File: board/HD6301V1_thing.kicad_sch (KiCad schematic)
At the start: 51 parts, among them J1 KMDGX-6S-BS, J2 ps2_i2c, J3 P1_connector, J4 memmap_i2c, J5 8bit_thing_bus_connector, J6 USB_B_Micro, J7 prog_LED, J8 pwr_LED, SW1 Reset, SW2 Banking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

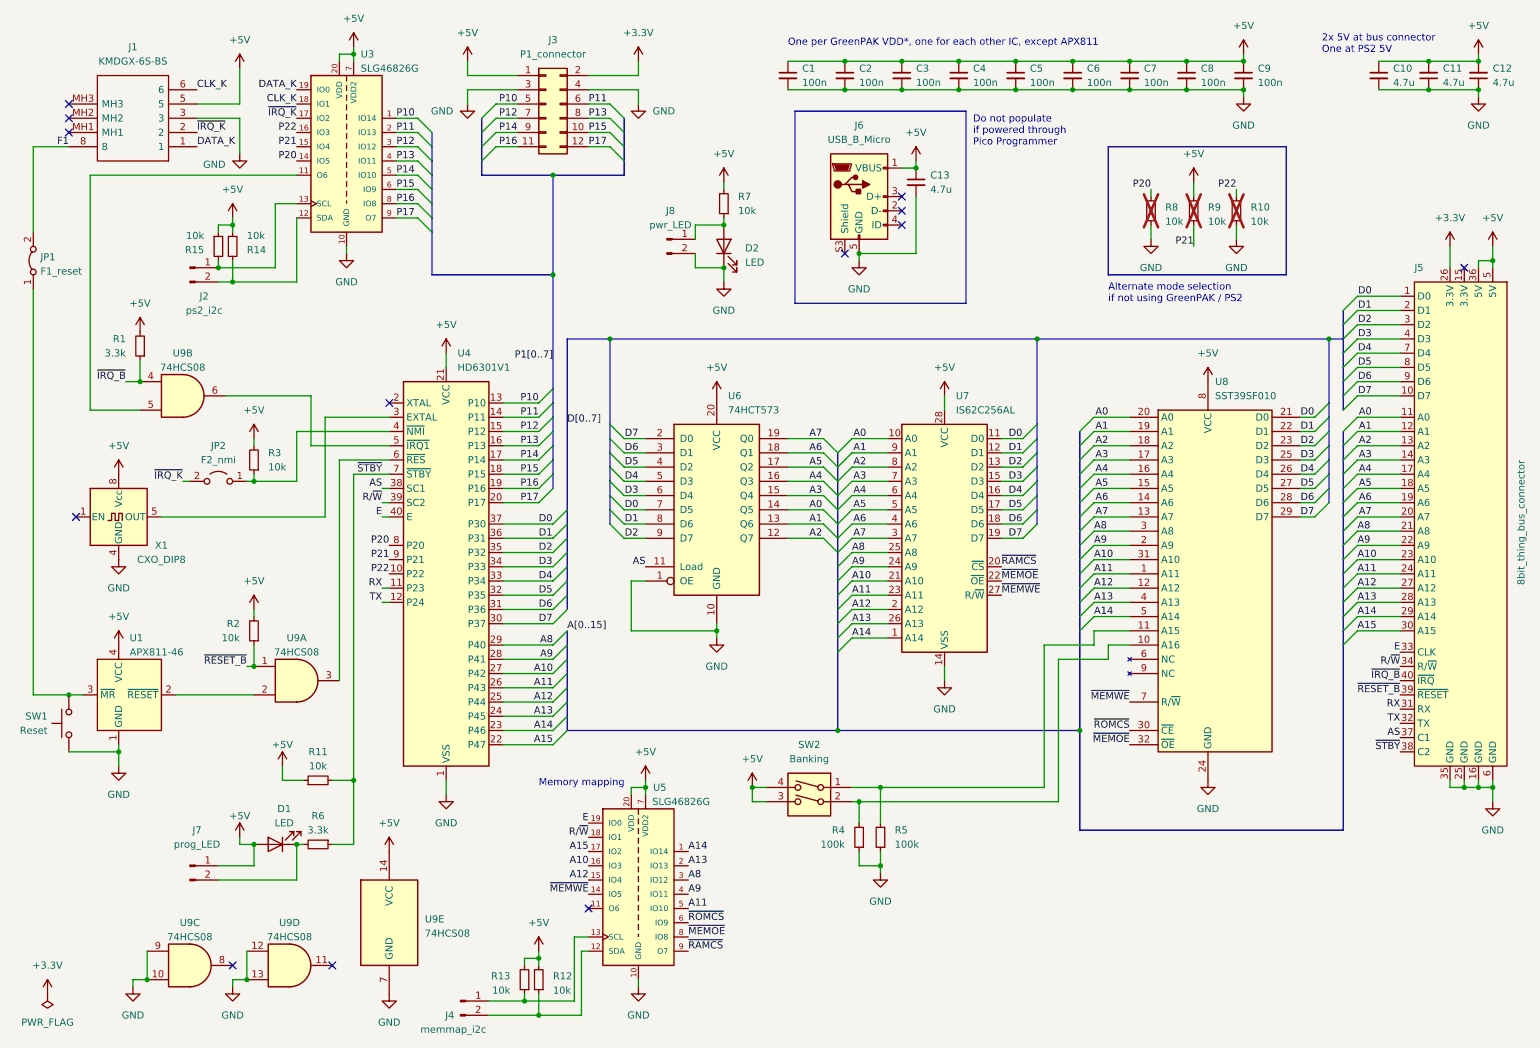
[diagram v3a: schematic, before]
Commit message: HD6301 board: tie address latch OE to standby
This makes the address latch let go of the bus on standby which simplifies the
pico programmer.
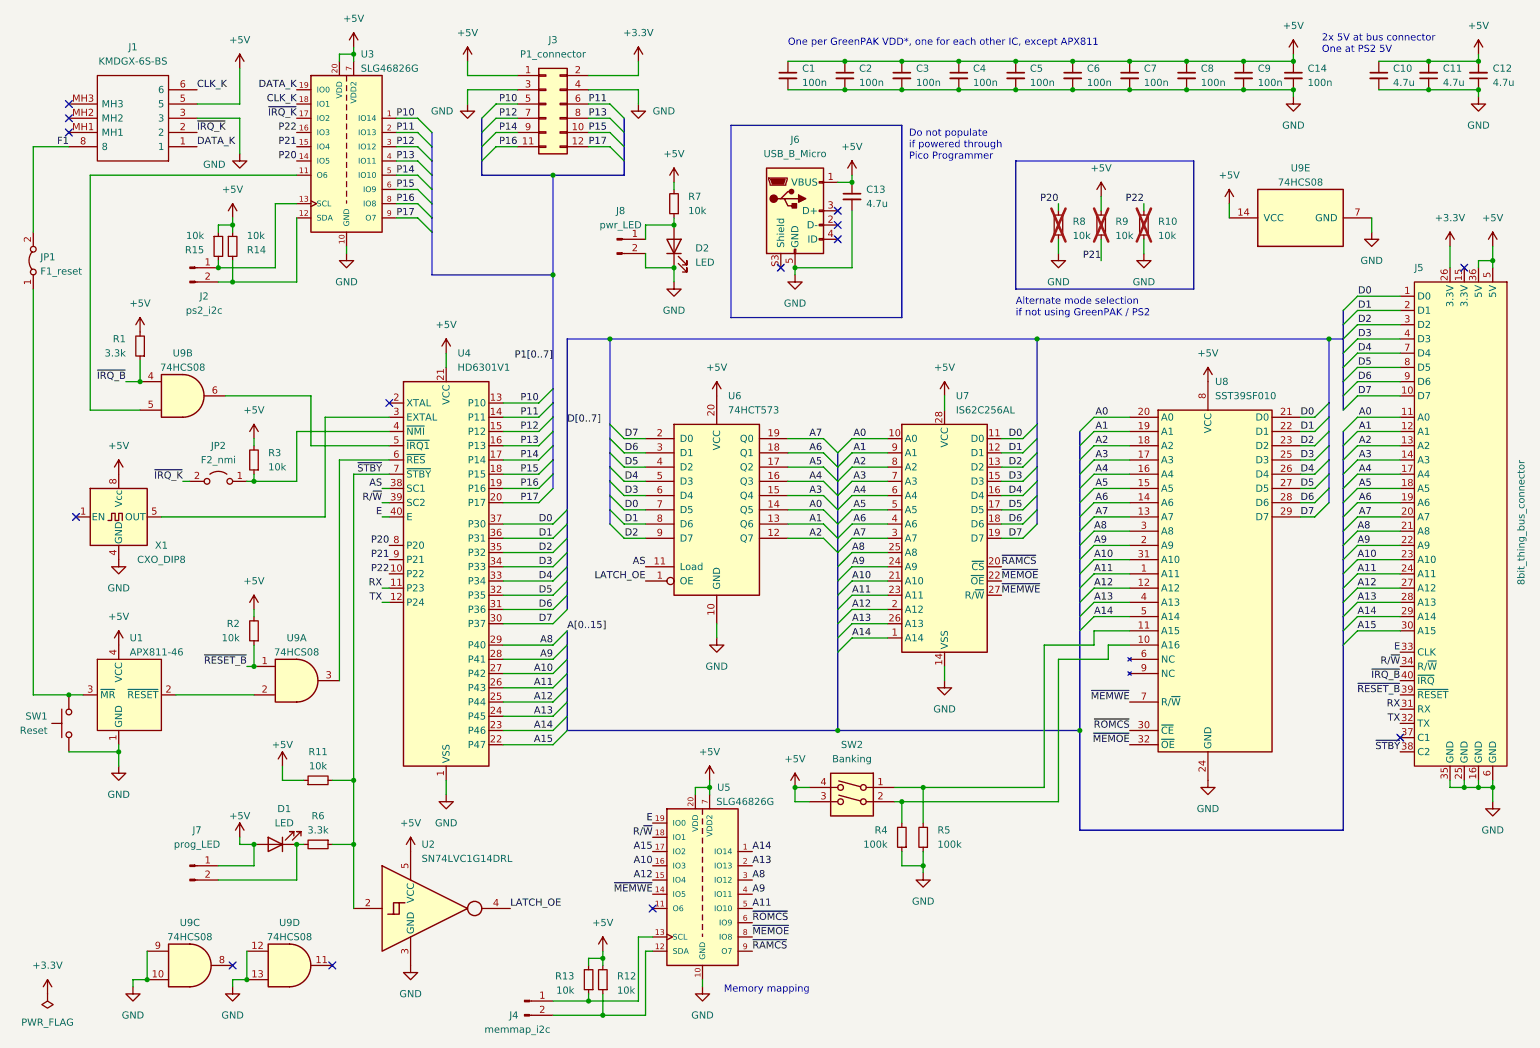
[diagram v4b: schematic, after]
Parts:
- added C14: 100n, Capacitor_SMD:C_0805_2012Metric_Pad1.18x1.45mm_HandSolder, symbol Device:C_Small
- added U2: SN74LVC1G14DRL, Package_TO_SOT_SMD:SOT-353_SC-70-5_Handsoldering, symbol 74xGxx:SN74LVC1G14DRL
- U1: footprint Package_TO_SOT_SMD:SOT-143 -> Package_TO_SOT_SMD:SOT-143_Handsoldering
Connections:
- net +5V: now also C14.1, U2.5 (VCC)
- net AS: no longer J5.37 (C1)
- net GND: now also C14.2, U2.3 (GND); no longer U6.1 (OE)
- net ~{STBY}: now also U2.2
- new net LATCH_OE: U2.4, U6.1 (OE)
- no-connect marks 13 -> 14
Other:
- moved on the sheet: C13, D2, J4, J6, J8, R10, R12, R13, R4, R5, R7, R8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

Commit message: Final version of HD6301V1 v1 board
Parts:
- added D3: BAT54W, Package_TO_SOT_SMD:SOT-323_SC-70_Handsoldering, symbol Diode:BAT54W
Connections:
- net CLK_K: now also U3.14 (IO5); no longer U3.18 (IO1)
- net DATA_K: now also U3.15 (IO4); no longer U3.19 (IO0)
- net P20: now also U3.17 (IO2); no longer U3.14 (IO5)
- net P21: now also U3.18 (IO1); no longer U3.15 (IO4)
- net P22: now also U3.19 (IO0); no longer U3.16 (IO3)
- net ~{IRQ_K}: now also U3.16 (IO3); no longer U3.17 (IO2)
- net ~{STBY}: now also D3.3 (K)
- net at JP1.1 (A), SW1.2, U1.3 (~{MR}): now also D3.1 (A)
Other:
- note added: "RESET needs to be asserted a bit longer than STBY to wait for the clock to stabilize."
- moved on the sheet: SW1
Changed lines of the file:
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@@
   (junction (at 264.16 24.13) (diameter 0) (color 0 0 0 0)
   )
+  (junction (at 22.86 137.16) (diameter 0) (color 0 0 0 0)
+  )
   (junction (at 170.18 24.13) (diameter 0) (color 0 0 0 0)
   )
@@
   (junction (at 118.11 73.66) (diameter 0) (color 0 0 0 0)
   )
+  (junction (at 72.39 140.97) (diameter 0) (color 0 0 0 0)
+  )
   (junction (at 170.18 156.21) (diameter 0) (color 0 0 0 0)
   )
@@
   (junction (at 129.54 60.96) (diameter 0) (color 0 0 0 0)
   )
-  (junction (at 21.59 137.16) (diameter 0) (color 0 0 0 0)
+  (junction (at 15.24 137.16) (diameter 0) (color 0 0 0 0)
   )
   (junction (at 264.16 29.21) (diameter 0) (color 0 0 0 0)
@@
     (stroke (width 0) (type default))
   )
-  (wire (pts (xy 21.59 137.16) (xy 24.13 137.16))
+  (wire (pts (xy 15.24 137.16) (xy 22.86 137.16))
     (stroke (width 0) (type default))
   )
@@
     (stroke (width 0) (type default))
   )
-  (wire (pts (xy 40.64 137.16) (xy 54.61 137.16))
-    (stroke (width 0) (type default))
-  )
   (bus (pts (xy 110.49 138.43) (xy 110.49 140.97))
     (stroke (width 0) (type default))
@@
     (stroke (width 0) (type default))
   )
+  (wire (pts (xy 43.18 140.97) (xy 72.39 140.97))
+    (stroke (width 0) (type default))
+  )
   (wire (pts (xy 92.71 26.67) (xy 101.6 26.67))
     (stroke (width 0) (type default))
@@
     (stroke (width 0) (type default))
   )
-  (wire (pts (xy 15.24 64.77) (xy 15.24 137.16))
-    (stroke (width 0) (type default))
-  )
   (wire (pts (xy 53.34 182.88) (xy 53.34 187.96))
     (stroke (width 0) (type default))
@@
     (stroke (width 0) (type default))
   )
-  (wire (pts (xy 15.24 137.16) (xy 21.59 137.16))
-    (stroke (width 0) (type default))
-  )
   (wire (pts (xy 161.29 44.45) (xy 161.29 45.72))
     (stroke (width 0) (type default))
@@
     (stroke (width 0) (type default))
   )
+  (wire (pts (xy 15.24 64.77) (xy 15.24 137.16))
+    (stroke (width 0) (type default))
+  )
   (bus (pts (xy 110.49 119.38) (xy 110.49 121.92))
     (stroke (width 0) (type default))
@@
     (stroke (width 0) (type default))
   )
+  (wire (pts (xy 15.24 157.48) (xy 16.51 157.48))
+    (stroke (width 0) (type default))
+  )
   (bus (pts (xy 201.93 92.71) (xy 201.93 90.17))
     (stroke (width 0) (type default))
@@
     (stroke (width 0) (type default))
   )
+  (wire (pts (xy 15.24 137.16) (xy 15.24 157.48))
+    (stroke (width 0) (type default))
+  )
   (wire (pts (xy 241.3 105.41) (xy 243.84 105.41))
     (stroke (width 0) (type default))
   )
+  (wire (pts (xy 22.86 137.16) (xy 24.13 137.16))
+    (stroke (width 0) (type default))
+  )
   (bus (pts (xy 248.92 123.19) (xy 248.92 125.73))
     (stroke (width 0) (type default))
@@
     (stroke (width 0) (type default))
   )
-  (wire (pts (xy 72.39 97.79) (xy 72.39 152.4))
+  (wire (pts (xy 72.39 97.79) (xy 72.39 140.97))
     (stroke (width 0) (type default))
   )
@@
     (stroke (width 0) (type default))
   )
+  (wire (pts (xy 24.13 157.48) (xy 43.18 157.48))
+    (stroke (width 0) (type default))
+  )
   (bus (pts (xy 107.95 87.63) (xy 107.95 90.17))
     (stroke (width 0) (type default))
@@
     (stroke (width 0) (type default))
   )
+  (wire (pts (xy 43.18 157.48) (xy 43.18 140.97))
+    (stroke (width 0) (type default))
+  )
   (bus (pts (xy 158.75 124.46) (xy 158.75 127))
     (stroke (width 0) (type default))
@@
     (stroke (width 0) (type default))
   )
+  (wire (pts (xy 40.64 137.16) (xy 54.61 137.16))
+    (stroke (width 0) (type default))
+  )
   (wire (pts (xy 210.82 113.03) (xy 204.47 113.03))
     (stroke (width 0) (type default))
@@
     (stroke (width 0) (type default))
   )
-  (wire (pts (xy 21.59 147.32) (xy 30.48 147.32))
+  (wire (pts (xy 22.86 147.32) (xy 30.48 147.32))
     (stroke (width 0) (type default))
   )
@@
     (stroke (width 0) (type default))
   )
+  (wire (pts (xy 72.39 140.97) (xy 72.39 152.4))
+    (stroke (width 0) (type default))
+  )
   (wire (pts (xy 187.96 101.6) (xy 191.77 101.6))
     (stroke (width 0) (type default))
@@
     (fill (type none))
   )
+  (text "RESET needs to be asserted\na bit longer than STBY\nto wait for the clock\nto stabilize."
+    (at 15.24 167.64 0)
+    (effects (font (size 1.27 1.27)) (justify left bottom))
+  )
   (text "Memory mapping" (at 138.43 190.5 0)
     (effects (font (size 1.27 1.27)) (justify left bottom))
@@
     (effects (font (size 1.27 1.27)) (justify right bottom))
   )
-  (label "P20" (at 62.23 41.91 180) (fields_autoplaced)
+  (label "P20" (at 62.23 34.29 180) (fields_autoplaced)
     (effects (font (size 1.27 1.27)) (justify right bottom))
   )
@@
     (effects (font (size 1.27 1.27)) (justify right bottom))
   )
-  (label "P22" (at 62.23 36.83 180) (fields_autoplaced)
+  (label "P22" (at 62.23 29.21 180) (fields_autoplaced)
     (effects (font (size 1.27 1.27)) (justify right bottom))
   )
@@
     (effects (font (size 1.27 1.27)) (justify left bottom))
   )
-  (label "~{IRQ_K}" (at 62.23 34.29 180) (fields_autoplaced)
+  (label "~{IRQ_K}" (at 62.23 36.83 180) (fields_autoplaced)
     (effects (font (size 1.27 1.27)) (justify right bottom))
   )
@@
     (effects (font (size 1.27 1.27)) (justify right bottom))
   )
-  (label "CLK_K" (at 62.23 31.75 180) (fields_autoplaced)
+  (label "CLK_K" (at 62.23 41.91 180) (fields_autoplaced)
     (effects (font (size 1.27 1.27)) (justify right bottom))
   )
@@
     (effects (font (size 1.27 1.27)) (justify right bottom))
   )
-  (label "DATA_K" (at 62.23 29.21 180) (fields_autoplaced)
+  (label "DATA_K" (at 62.23 39.37 180) (fields_autoplaced)
     (effects (font (size 1.27 1.27)) (justify right bottom))
   )
@@
     (effects (font (size 1.27 1.27)) (justify right bottom))
   )
-  (label "P21" (at 62.23 39.37 180) (fields_autoplaced)
+  (label "P21" (at 62.23 31.75 180) (fields_autoplaced)
     (effects (font (size 1.27 1.27)) (justify right bottom))
   )
@@
     )
   )
+  (symbol (lib_id "Diode:BAT54W") (at 20.32 157.48 180) (unit 1)
+    (in_bom yes) (on_board yes) (dnp no) (fields_autoplaced)
+    (property "Reference" "D3" (at 20.6375 152.4 0)
+      (effects (font (size 1.27 1.27)))
+    )
+    (property "Value" "BAT54W" (at 20.6375 154.94 0)
+      (effects (font (size 1.27 1.27)))
+    )
+    (property "Footprint" "Package_TO_SOT_SMD:SOT-323_SC-70_Handsoldering" (at 20.32 153.035 0)
+      (effects (font (size 1.27 1.27)) hide)
+    )
+    (property "Datasheet" "https://assets.nexperia.com/documents/data-sheet/BAT54W_SER.pdf" (at 20.32 157.48 0)
+      (effects (font (size 1.27 1.27)) hide)
+    )
+    (pin "1")
+    (pin "2")
+    (pin "3")
+    (instances
+      (project "HD6301V1_thing"
+        (path "/f94fb884-8365-431c-b8b6-ec4493810111"
+          (reference "D3") (unit 1)
+        )
+      )
+    )
+  )
   (symbol (lib_id "74xx:74LS08") (at 41.91 83.82 0) (unit 2)
     (in_bom yes) (on_board yes) (dnp no) (fields_autoplaced)
@@
     )
   )
-  (symbol (lib_id "Switch:SW_Push") (at 21.59 142.24 90) (unit 1)
-    (in_bom yes) (on_board yes) (dnp no) (fields_autoplaced)
-    (property "Reference" "SW1" (at 17.78 140.9699 90)
+  (symbol (lib_id "Switch:SW_Push") (at 22.86 142.24 90) (unit 1)
+    (in_bom yes) (on_board yes) (dnp no)
+    (property "Reference" "SW1" (at 19.05 140.9699 90)
       (effects (font (size 1.27 1.27)) (justify left))
     )
-    (property "Value" "Reset" (at 17.78 143.5099 90)
+    (property "Value" "Reset" (at 19.05 143.5099 90)
       (effects (font (size 1.27 1.27)) (justify left))
     )
-    (property "Footprint" "Button_Switch_SMD:SW_SPST_TL3305A" (at 16.51 142.24 0)
+    (property "Footprint" "Button_Switch_SMD:SW_SPST_TL3305A" (at 17.78 142.24 0)
       (effects (font (size 1.27 1.27)) hide)
     )
-    (property "Datasheet" "~" (at 16.51 142.24 0)
+    (property "Datasheet" "~" (at 17.78 142.24 0)
       (effects (font (size 1.27 1.27)) hide)
     )

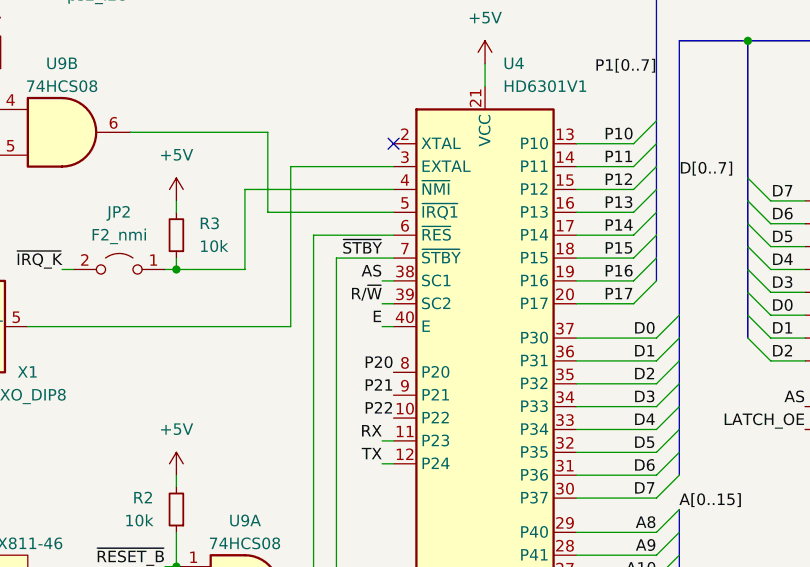
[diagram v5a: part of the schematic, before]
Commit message: HD6301 board: fix swapped SC1/SC2 pins
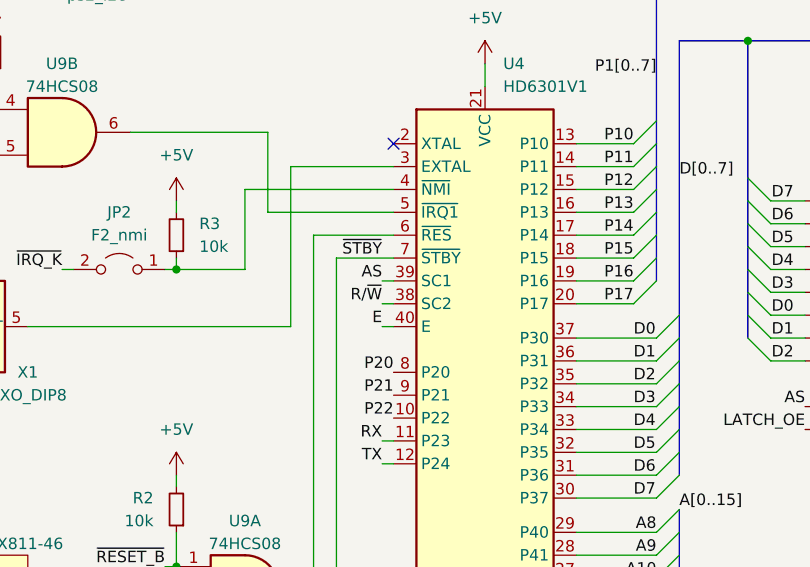
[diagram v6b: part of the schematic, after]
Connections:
- net AS: now also U4.39 (SC1); no longer U4.38 (SC1)
- net R/~{W}: now also U4.38 (SC2); no longer U4.39 (SC2)
